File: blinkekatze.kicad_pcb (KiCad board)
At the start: 4 copper layers, 68.1 x 69 mm, 114 parts, among them J1 Power key, J2 Conn_01x06, Q1 AO3400A, Q2 AO3400A, U1 ESP32-C3-MINI-1, U10 LIS3DH, U2 BQ27546, U3 SRV05-4, U4 FM2113, U5 SPL06-001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

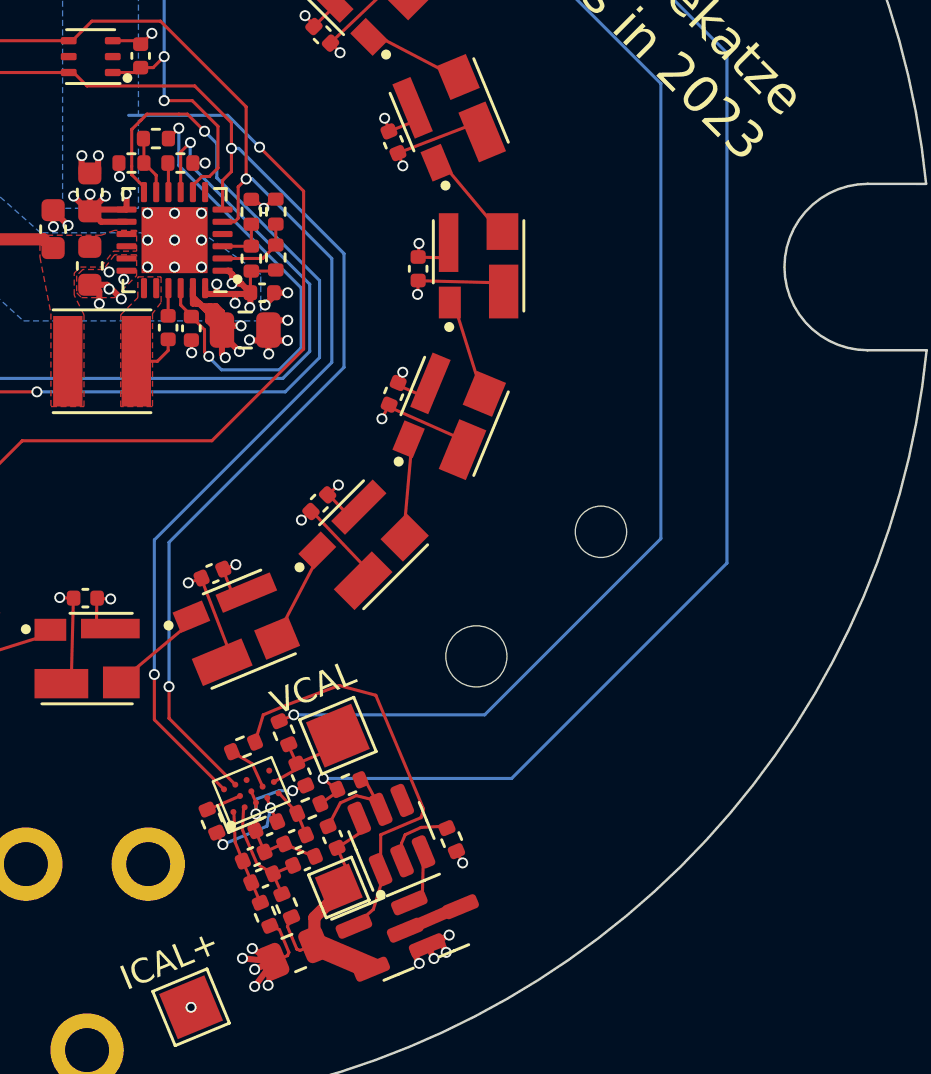
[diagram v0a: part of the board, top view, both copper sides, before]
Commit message: Add I2C test connector
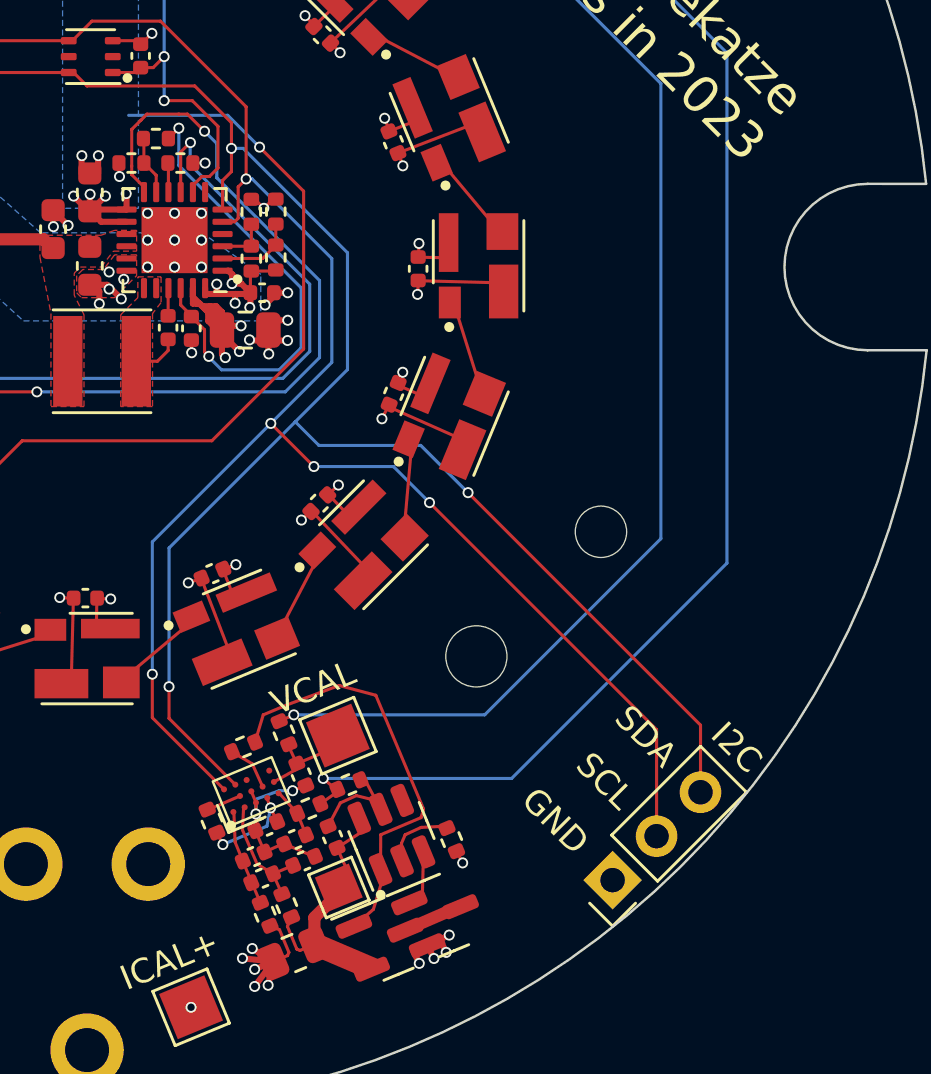
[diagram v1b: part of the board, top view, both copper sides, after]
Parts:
- added J3: I2C, Connector_PinHeader_2.54mm:PinHeader_1x03_P2.54mm_Vertical, F.Cu at (121.5, 125.1)
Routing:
- net /Battery/SCL: track 79.4 -> 104.8 mm, vias 4 -> 7
- net /Battery/SDA: track 78.1 -> 102.7 mm, vias 6 -> 7
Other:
- board text added: "I2C"
- board text added: "SCL"
- board text added: "SDA"

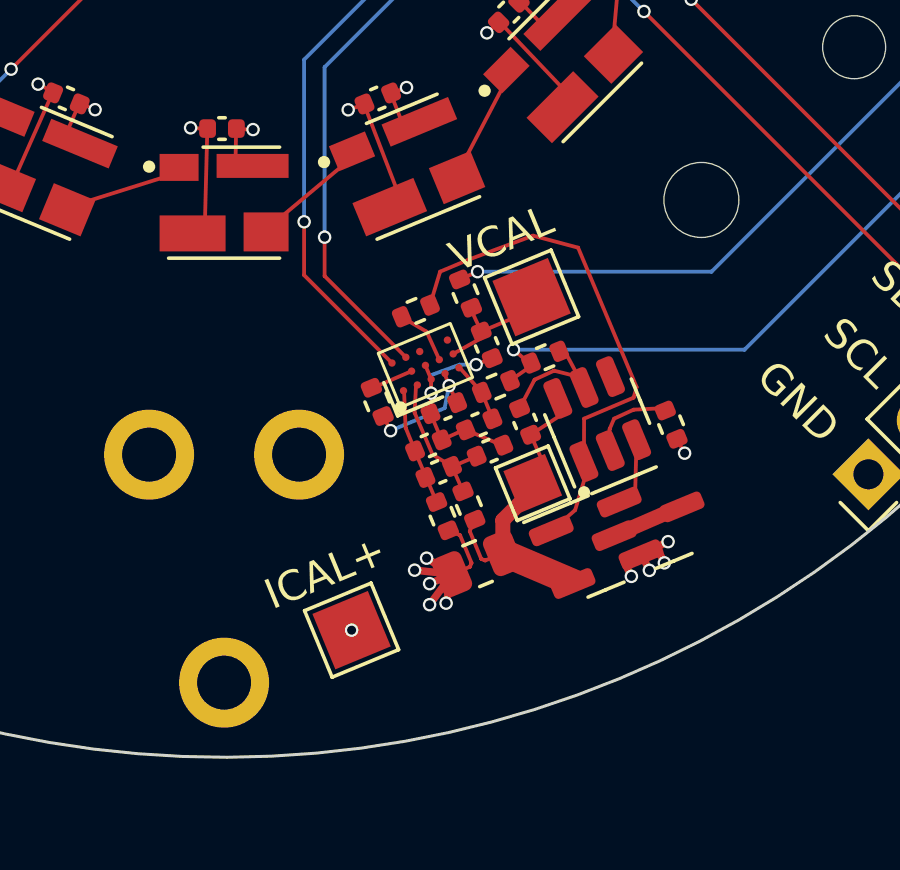
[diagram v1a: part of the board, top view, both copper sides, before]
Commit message: Add battery polarity indicators
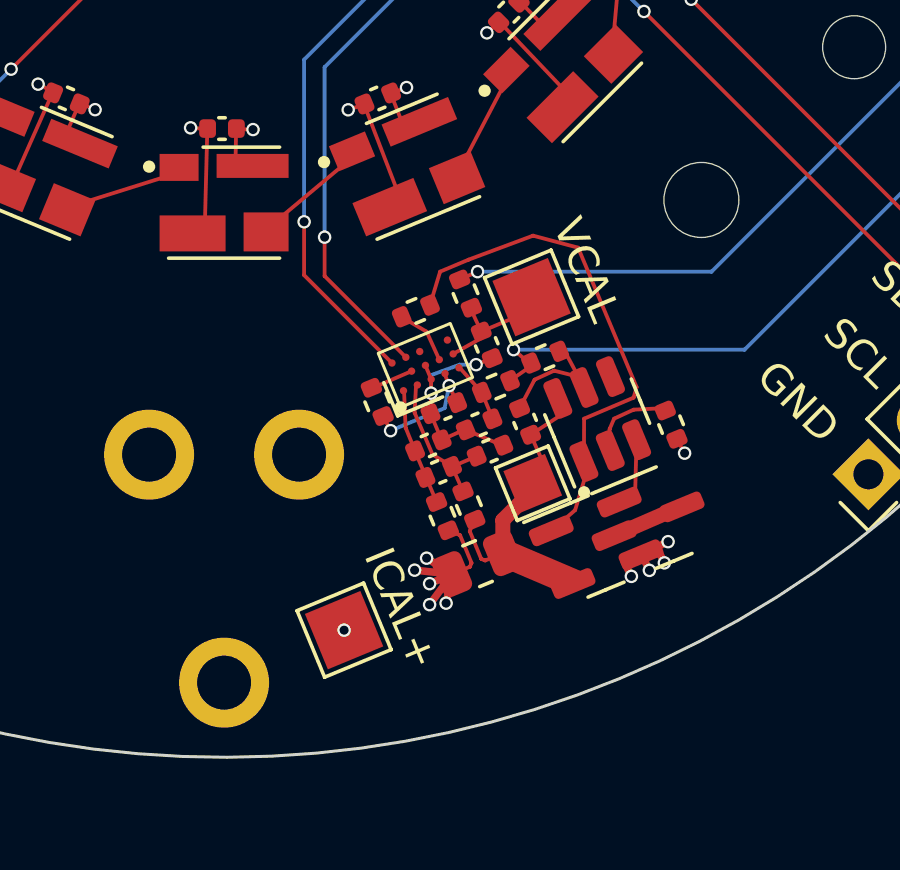
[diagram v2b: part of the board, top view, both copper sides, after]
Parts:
- moved TP3 0.25 mm to (104.0, 130.2)
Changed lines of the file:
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@@
   )
   (footprint "TestPoint:TestPoint_Pad_2.0x2.0mm" (layer "F.Cu")
-    (at 104.25 130.25 22.5)
+    (at 104 130.25 22.5)
     (descr "SMD rectangular pad as test Point, square 2.0mm side length")
     (tags "test point SMD pad rectangle square")
@@
     )
   )
+  (gr_line (start 111 71) (end 111 75)
+    (stroke (width 0.3) (type default)) (layer "B.SilkS"))
+  (gr_line (start 109 128) (end 113 128)
+    (stroke (width 0.3) (type default)) (layer "B.SilkS"))
+  (gr_line (start 109 73) (end 113 73)
+    (stroke (width 0.3) (type default)) (layer "B.SilkS"))
   (gr_circle (center 91.9 71.1) (end 92.1 71.1)
     (stroke (width 0.001) (type solid)) (fill solid) (layer "F.SilkS"))
@@
     (effects (font (size 1 1) (thickness 0.15)) (justify right))
   )
-  (gr_text "ICAL+" (at 101.65 129.675 22.5) (layer "F.SilkS")
+  (gr_text "ICAL+" (at 104.55 127.8 -67.5) (layer "F.SilkS")
     (effects (font (size 1 1) (thickness 0.15)) (justify left bottom))
   )
@@
     (effects (font (size 1 1) (thickness 0.15)))
   )
-  (gr_text "VCAL" (at 107.8 118.425 22.5) (layer "F.SilkS")
+  (gr_text "VCAL" (at 110.85 116.8 -67.5) (layer "F.SilkS")
     (effects (font (size 1 1) (thickness 0.15)) (justify left bottom))
   )
@@
   (via (at 106.75 127.85) (size 0.45) (drill 0.3) (layers "F.Cu" "B.Cu") (net 2))
   (via (at 107.4 129.35) (size 0.45) (drill 0.3) (layers "F.Cu" "B.Cu") (net 2))
-  (via (at 104.25 130.25) (size 0.45) (drill 0.3) (layers "F.Cu" "B.Cu") (net 2))
+  (via (at 104 130.25) (size 0.45) (drill 0.3) (layers "F.Cu" "B.Cu") (net 2))
   (via (at 106.9 122.35) (size 0.45) (drill 0.3) (layers "F.Cu" "B.Cu") (net 2))
   (via (at 106.85 128.7) (size 0.45) (drill 0.3) (layers "F.Cu" "B.Cu") (net 2))

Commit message: Update SK6812-MINI-X1 footprints
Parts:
- R11: value 470R -> 100R
